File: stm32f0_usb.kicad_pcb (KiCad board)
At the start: 2 copper layers, 70 x 50 mm, 41 parts, among them J1 USB_B_Mini, J2 Conn_ARM_JTAG_SWD_10, J3 Conn_01x14_Male, J4 Conn_01x14_Male, SW1 B3S-1000P, SW2 B3S-1000P, U1 STM32F042K6Tx, U2 ADP121-AUJZ33R7, U3 USBLC6-2SC6, X1 ASV-8.000MHz

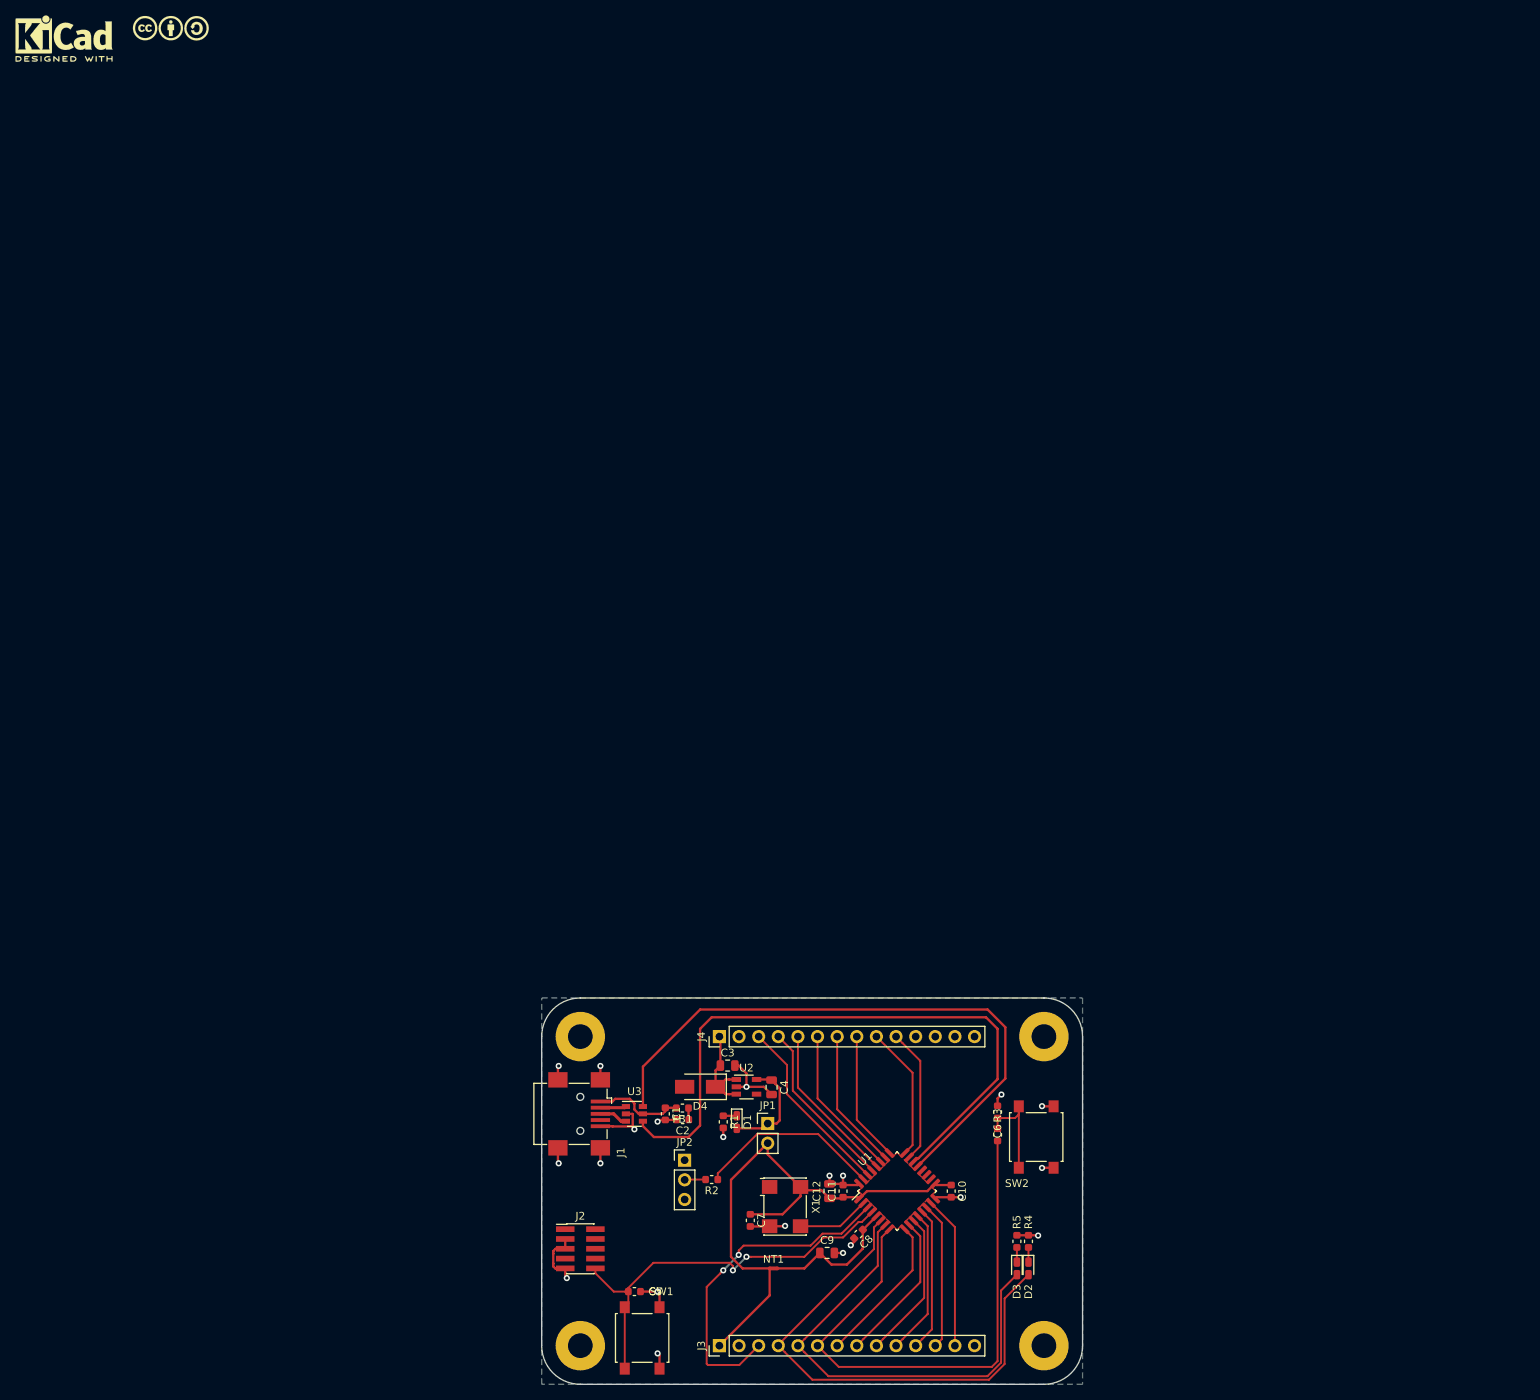
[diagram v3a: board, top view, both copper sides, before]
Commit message: complete routing
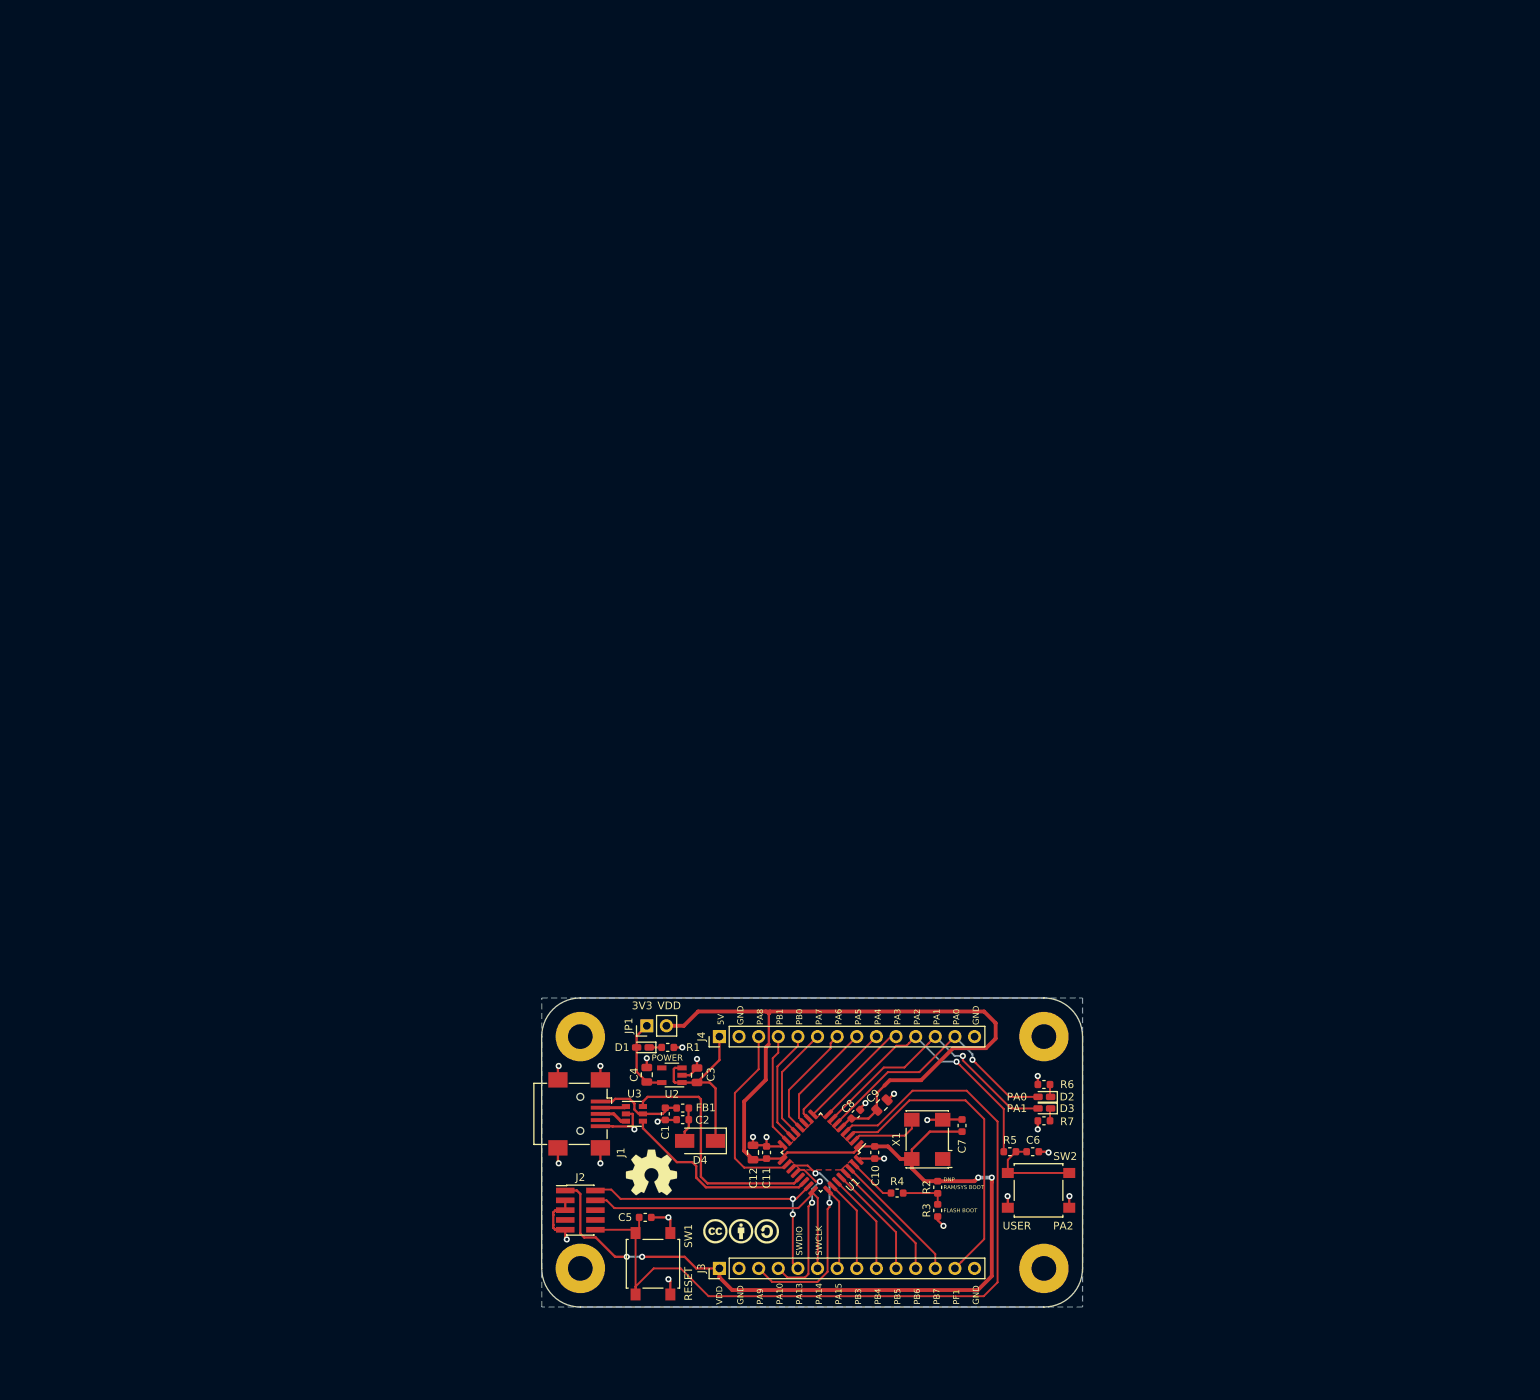
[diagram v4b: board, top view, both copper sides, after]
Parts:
- removed JP2: Jumper_3_Bridged12, Connector_PinHeader_2.54mm:PinHeader_1x03_P2.54mm_Vertical
- added LOGO3: Logo_Open_Hardware_Small, Symbol:OSHW-Symbol_6.7x6mm_SilkScreen, F.Cu at (114.2, 122.6)
- added R3: 0, Resistor_SMD:R_0603_1608Metric, F.Cu at (151.2, 127.5)
- added R4: 10k, Resistor_SMD:R_0603_1608Metric, F.Cu at (146.0, 125.2)
- LOGO1: moved to B.Cu
- R2: value 10k -> 0 DNP
- moved LOGO1 186.7 mm to (144.6, 129.2), turned to 180 degrees
- moved LOGO2 172.3 mm to (125.8, 130.2)
- moved C7 30.0 mm to (154.4, 116.5), turned to 90 degrees
- moved R2 29.3 mm to (151.2, 124.5), turned to 90 degrees
- moved NT1 28.1 mm to (144.7, 111.0), turned to 225 degrees
- moved D2 22.3 mm to (165.1, 112.8), turned to 180 degrees
- moved D3 21.0 mm to (165.1, 114.3), turned to 180 degrees
- moved C9 20.4 mm to (144.0, 113.9), turned to 45 degrees
- moved R6 20.4 mm to (165.0, 111.2), turned to 180 degrees
- moved X1 20.4 mm to (149.9, 118.3), turned to 90 degrees
- moved JP1 20.1 mm to (113.6, 103.6), turned to 90 degrees
- moved C4 16.2 mm to (113.6, 109.9), turned to 90 degrees
- moved R7 16.0 mm to (165.0, 115.9), turned to 180 degrees
- moved D1 15.5 mm to (113.1, 106.4), turned to 180 degrees
- moved C8 15.5 mm to (140.7, 115.0), turned to 45 degrees
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- renumbered R3 to R5, R4 to R6, R5 to R7
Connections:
- J3 pad 10: /STM32/PA6 -> /STM32/PB5
- J3 pad 11: /STM32/PA7 -> /STM32/PB6
- J3 pad 12: /STM32/PB0 -> /STM32/PB7
- J3 pad 13: /STM32/PB1 -> /STM32/PF1
- J3 pad 3: /STM32/PF1 -> /STM32/PA9
- J3 pad 4: /STM32/PA0 -> /STM32/PA10
- J3 pad 5: /STM32/PA1 -> /STM32/PA13_SWDIO
- J3 pad 6: /STM32/PA2 -> /STM32/PA14_SWCLK
- J3 pad 7: /STM32/PA3 -> /STM32/PA15
- J3 pad 8: /STM32/PA4 -> /STM32/PB3
- J3 pad 9: /STM32/PA5 -> /STM32/PB4
- J4 pad 10: /STM32/PA13_SWDIO -> /STM32/PA3
- J4 pad 11: /STM32/PA10 -> /STM32/PA2
- J4 pad 12: /STM32/PA9 -> /STM32/PA1
- J4 pad 13: /STM32/PA8 -> /STM32/PA0
- J4 pad 3: /STM32/PB7 -> /STM32/PA8
- J4 pad 4: /STM32/PB6 -> /STM32/PB1
- J4 pad 5: /STM32/PB5 -> /STM32/PB0
- J4 pad 6: /STM32/PB4 -> /STM32/PA7
- J4 pad 7: /STM32/PB3 -> /STM32/PA6
- J4 pad 8: /STM32/PA15 -> /STM32/PA5
- J4 pad 9: /STM32/PA14_SWCLK -> /STM32/PA4
- R2 pad 1: /STM32/BOOT0 -> Net-(R2-Pad1)
- R2 pad 2: Net-(JP2-Pad2) -> VDD
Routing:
- net VDD: track 72.3 -> 205.0 mm, vias 0 -> 4
- net /STM32/NRST: track 53.3 -> 111.0 mm, vias 2 -> 0
- net /STM32/USB_DP: track 83.3 -> 26.1 mm
- net /STM32/USB_DM: track 78.7 -> 32.1 mm
- net /STM32/PA2: track 72.2 -> 36.3 mm, vias 0 -> 1
- net /STM32/PA0: track 66.5 -> 34.3 mm, vias 0 -> 1
- net /STM32/PA9: track 0.00 -> 27.9 mm, vias 0 -> 2
- net /STM32/PA1: track 61.2 -> 35.2 mm, vias 0 -> 1
- net /STM32/PA8: track 0.00 -> 24.4 mm
- net /STM32/PA14_SWCLK: track 17.4 -> 39.7 mm
- net /STM32/PA10: track 0.00 -> 21.1 mm, vias 0 -> 2
- net /STM32/PA13_SWDIO: track 17.5 -> 38.5 mm, vias 0 -> 2
- net /STM32/BOOT0: track 24.2 -> 6.28 mm
- net +5V: track 12.6 -> 22.4 mm
- net VDDA: track 18.3 -> 9.11 mm
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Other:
- board size 70 x 50 mm -> 70 x 40 mm
- board text added: "STM32F0 USB Dev Board G. Keeth 2020-01-12 https://github.com/gkeeth/stm32f0_usb_basic"
- board text added: "TODO pinout table?"
- board text removed: "TODO move USB connector? redo vdd-vdda routing move BOOT0 jumper"

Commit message: fatten power traces, add pinout table, neaten silk
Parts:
- moved LOGO1 2.00 mm to (146.6, 129.2)
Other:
- board text added: "PA0 LED0 PA1 LED1 PA2 BUT PA3 ADC_IN3 PA4 ADC_IN4 PA5 ADC_IN5 PA6 ADC_IN6 PA7 ADC_IN7 PA8 PA9 PA10"
- board text added: "PA13 SWDIO PA14 SWCLK PA15 PB0 ADC_IN8 PB1 ADC_IN9 PB3 PB4 PB5 PB6 PB7 PF1"
- board text removed: "TODO pinout table?"
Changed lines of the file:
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@@
   (general
     (thickness 1.6)
-    (drawings 10)
+    (drawings 11)
     (tracks 385)
     (zones 0)
@@
     (0 F.Cu signal)
     (31 B.Cu signal)
-    (32 B.Adhes user)
-    (33 F.Adhes user)
+    (32 B.Adhes user hide)
+    (33 F.Adhes user hide)
     (34 B.Paste user)
     (35 F.Paste user)
@@
   )
   (module Symbol:KiCad-Logo2_5mm_SilkScreen (layer B.Cu)
-    (at 144.6 129.2 180)
+    (at 146.6 129.2 180)
     (descr "KiCad Logo")
     (tags "Logo KiCad")
@@
     )
   )
-  (gr_text "STM32F0 USB Dev Board\nG. Keeth\n2020-01-12\nhttps://github.com/gkeeth/stm32f0_usb_basic" (at 140 112) (layer B.SilkS)
-    (effects (font (size 1 1) (thickness 0.15)) (justify left mirror))
-  )
-  (gr_text "TODO\npinout table?" (at 182.2 112.8) (layer Cmts.User)
-    (effects (font (size 1 1) (thickness 0.15)) (justify left))
+  (gr_text "PA13  SWDIO\nPA14  SWCLK\nPA15\nPB0   ADC_IN8\nPB1   ADC_IN9\nPB3\nPB4\nPB5\nPB6\nPB7\nPF1" (at 124 114) (layer B.SilkS)
+    (effects (font (size 0.8 0.8) (thickness 0.12)) (justify left mirror))
+  )
+  (gr_text "PA0  LED0\nPA1  LED1\nPA2  BUT\nPA3  ADC_IN3\nPA4  ADC_IN4\nPA5  ADC_IN5\nPA6  ADC_IN6\nPA7  ADC_IN7\nPA8\nPA9\nPA10\n" (at 140 114) (layer B.SilkS)
+    (effects (font (size 0.8 0.8) (thickness 0.12)) (justify left mirror))
+  )
+  (gr_text "STM32F0 USB Dev Board\nG. Keeth\n2020-01-12\nhttps://github.com/gkeeth/stm32f0_usb_basic" (at 138 129.6) (layer B.SilkS)
+    (effects (font (size 0.8 0.8) (thickness 0.12)) (justify left mirror))
   )
   (gr_line (start 100 105) (end 100 135) (layer Edge.Cuts) (width 0.05))
